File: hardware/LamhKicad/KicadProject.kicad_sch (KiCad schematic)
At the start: 45 parts, among them J1 JTAG-10 PIN, J2 436500303, J3 436500303, J4 436500303, J5 ESQ-110-X-X-D, J6 436500303, U1 TJA1051T-3, U2 PCA9685PW_112, U3 TLV70433DBVT, U4 STM32F072C8Tx

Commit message: ready to route
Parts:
- added C18, C19, C20: 1000uf 16v, Capacitor_THT:CP_Radial_D10.0mm_P5.00mm, symbol Device:C_Polarized_US
- C16: value 4700uf 16v -> 1000uf 16v; footprint (none) -> Capacitor_THT:CP_Radial_D10.0mm_P5.00mm
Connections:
- net 5v_SERVO: now also C18.1, C19.1, C20.1
- net GND: now also C18.2, C19.2, C20.2
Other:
- moved on the sheet: C16, J1

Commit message: fixed the connector
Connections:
- net NRST4: no longer J5.12
- net SWCLK: no longer J5.17
- new net NRST: J5.17
- new net SWCLK4: J5.12
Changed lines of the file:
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@@
-		)
-	)
-	(global_label "NRST2"
-		(shape input)
-		(at 195.58 198.12 0)
-		(fields_autoplaced yes)
-		(effects
-			(font
-				(size 1.27 1.27)
-			)
-			(justify left)
-		)
-		(property "Intersheetrefs" "${INTERSHEET_REFS}"
-			(at 204.5523 198.12 0)
-			(effects
-				(font
-					(size 1.27 1.27)
-				)
-				(justify left)
-				(hide yes)
-			)
 		)
 	)
@@
 		)
 	)
-	(global_label "NRST3"
-		(shape input)
-		(at 167.64 200.66 180)
-		(fields_autoplaced yes)
-		(effects
-			(font
-				(size 1.27 1.27)
-			)
-			(justify right)
-		)
-		(property "Intersheetrefs" "${INTERSHEET_REFS}"
-			(at 158.6677 200.66 0)
-			(effects
-				(font
-					(size 1.27 1.27)
-				)
-				(justify right)
-				(hide yes)
-			)
-		)
-	)
 	(global_label "3.3V"
 		(shape input)
@@
 		)
 	)
-	(global_label "NRST5"
-		(shape input)
-		(at 167.64 203.2 180)
-		(fields_autoplaced yes)
-		(effects
-			(font
-				(size 1.27 1.27)
-			)
-			(justify right)
-		)
-		(property "Intersheetrefs" "${INTERSHEET_REFS}"
-			(at 158.6677 203.2 0)
-			(effects
-				(font
-					(size 1.27 1.27)
-				)
-				(justify right)
-				(hide yes)
-			)
-		)
-	)
 	(global_label "MOSI"
 		(shape input)
@@
 		)
 	)
+	(global_label "NRST"
+		(shape input)
+		(at 168.91 208.28 180)
+		(fields_autoplaced yes)
+		(effects
+			(font
+				(size 1.27 1.27)
+			)
+			(justify right)
+		)
+		(property "Intersheetrefs" "${INTERSHEET_REFS}"
+			(at 161.1472 208.28 0)
+			(effects
+				(font
+					(size 1.27 1.27)
+				)
+				(justify right)
+				(hide yes)
+			)
+		)
+	)
 	(global_label "SWCLK"
 		(shape input)
-		(at 168.91 208.28 180)
-		(fields_autoplaced yes)
-		(effects
-			(font
-				(size 1.27 1.27)
-			)
-			(justify right)
-		)
-		(property "Intersheetrefs" "${INTERSHEET_REFS}"
-			(at 159.6958 208.28 0)
-			(effects
-				(font
-					(size 1.27 1.27)
-				)
-				(justify right)
-				(hide yes)
-			)
-		)
-	)
-	(global_label "SWCLK"
-		(shape input)
 		(at 243.84 106.68 180)
 		(fields_autoplaced yes)
@@
 		)
 	)
-	(global_label "NRST1"
-		(shape input)
-		(at 167.64 198.12 180)
-		(fields_autoplaced yes)
-		(effects
-			(font
-				(size 1.27 1.27)
-			)
-			(justify right)
-		)
-		(property "Intersheetrefs" "${INTERSHEET_REFS}"
-			(at 158.6677 198.12 0)
-			(effects
-				(font
-					(size 1.27 1.27)
-				)
-				(justify right)
-				(hide yes)
-			)
-		)
-	)
 	(global_label "3.3V"
 		(shape input)
@@
 		)
 	)
-	(global_label "NRST4"
+	(global_label "SWCLK4"
 		(shape input)
 		(at 194.31 200.66 0)
@@
 		)
 		(property "Intersheetrefs" "${INTERSHEET_REFS}"
-			(at 203.2823 200.66 0)
-			(effects
-				(font
+			(at 204.7337 200.66 0)
+			(effects
+				(font

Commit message: minor changes
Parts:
- added R14, R15: 10kΩ, Resistor_SMD:R_0402_1005Metric, symbol Device:R
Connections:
- net 3.3V: now also R15.2
- net GND: now also R14.2
- net NRST: now also U4.7 (NRST), R15.1
- net NRST4: no longer U4.7 (NRST)
- net at U4.44 (BOOT0): now also R14.1

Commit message: minor changes
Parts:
- removed R15: 10kΩ, Resistor_SMD:R_0402_1005Metric, symbol Device:R
- added C21: 100nF, Capacitor_SMD:C_0402_1005Metric, symbol Device:C
- added C27, C28: 8pF, Capacitor_SMD:C_0402_1005Metric, symbol Device:C
- added XTAL1: NX3225GD-8MHZ-STD-CRA-3, XTAL_NX3225GD-8MHZ-STD-CRA-3_NDK, symbol STDCRA38M:NX3225GD-8MHZ-STD-CRA-3
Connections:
- net CAN_o+ is gone; now on net CAN_+: J5.16
- net CAN_o- is gone; now on net CAN_-: J5.18
- net NRST4 is gone; now on net NRST: J1.1 (Pin_1)
- net SWCLK is gone; now on net SWCLK4: J1.2 (Pin_2), U4.3 (PC14)
- net CAN_+: no longer U1.1 (TXD), U4.33 (PA12)
- net CAN_-: no longer U1.4 (RXD), U4.32 (PA11)
- net GND: now also C21.2, C27.1, C28.2
- net NRST: now also C21.1
- net at R3.1: now also J2.1; no longer J4.1
- net at R3.2: now also U2.10 (LED4); no longer U2.8 (LED2)
- net at U4.5 (PF0): now also C27.2, XTAL1.1
- net at U4.6 (PF1): now also C28.1, XTAL1.2
- net at U2.12 (LED6): now also R6.2
- net at U2.7 (LED1): no longer R2.2
- net at U2.9 (LED3): no longer R6.2
- net at R1.1: now also J4.1; no longer J2.1
- net at J3.1: now also R6.1; no longer R2.1
- net at J6.1: now also R2.1; no longer R6.1
- net ADC: no longer names the net of U4.14 (PA4)
- net CLK: no longer names the net of U4.15 (PA5)
- net CS: no longer names the net of U4.11 (PA1)
- net MISO: no longer names the net of U4.16 (PA6)
- net MOSI: no longer names the net of U4.17 (PA7)
- net OE: no longer names the net of U4.12 (PA2)
- net RESET: no longer names the net of U4.13 (PA3)
- new net: R2.2, U2.8 (LED2)
- new net CAN_e+: U1.1 (TXD), U4.33 (PA12)
- new net CAN_e-: U1.4 (RXD), U4.32 (PA11)
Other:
- moved on the sheet: J1

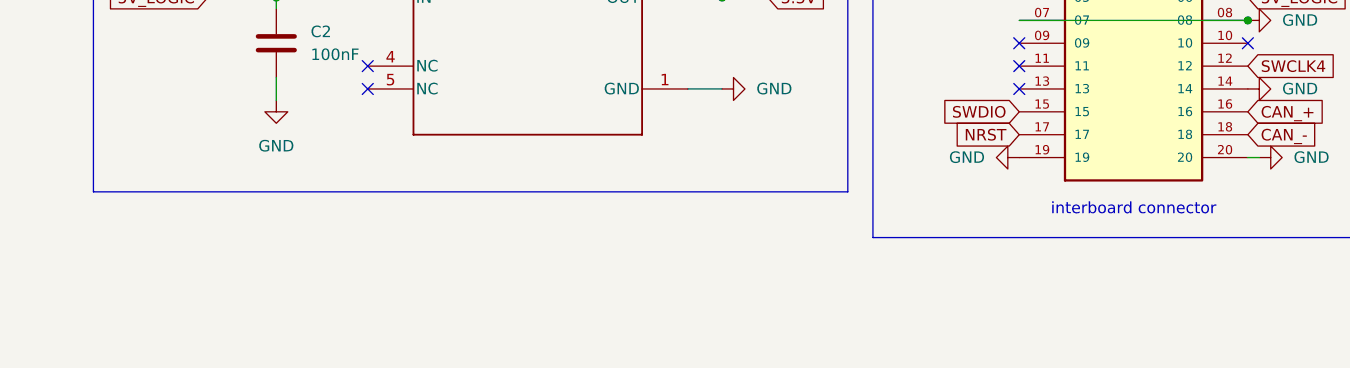
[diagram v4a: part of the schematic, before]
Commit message: added links to servo connectors
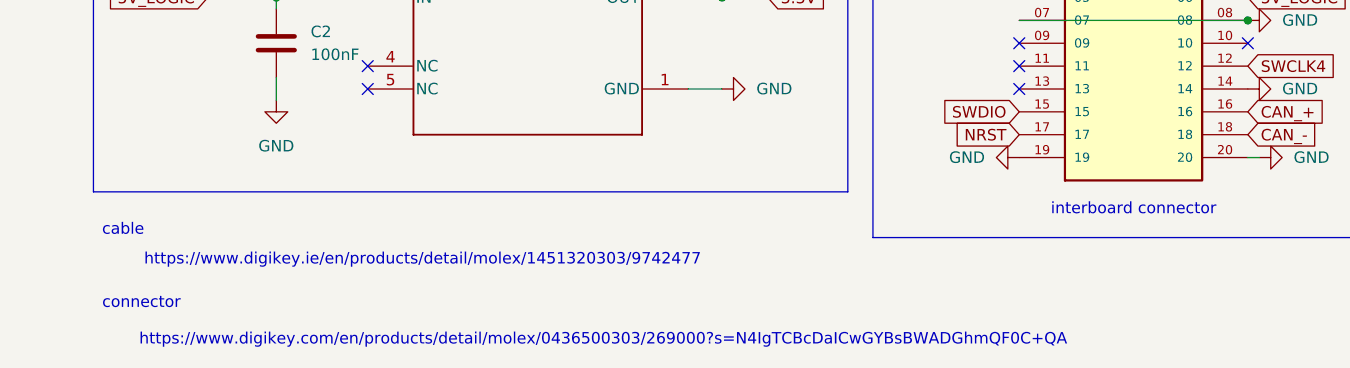
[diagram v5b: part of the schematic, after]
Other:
- note added: "cable"
- note added: "connector"
- note added: "https://www.digikey.com/en/products/detail/molex/0436500303/269000?s=N4IgTCBcDaICwGYBsBWADGhmQF0C+QA"
- note added: "https://www.digikey.ie/en/products/detail/molex/1451320303/9742477"
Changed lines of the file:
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@@
+		)
+	)
+	(text "cable\n"
+		(exclude_from_sim no)
+		(at 69.342 218.948 0)
+		(effects
+			(font
+				(size 1.27 1.27)
+			)
 		)
 	)
@@
 		(effects
 			(font
+				(size 1.27 1.27)
+			)
+		)
+	)
+	(text "https://www.digikey.com/en/products/detail/molex/0436500303/269000?s=N4IgTCBcDaICwGYBsBWADGhmQF0C+QA"
+		(exclude_from_sim no)
+		(at 122.682 231.14 0)
+		(effects
+			(font
+				(size 1.27 1.27)
+			)
+		)
+	)
+	(text "https://www.digikey.ie/en/products/detail/molex/1451320303/9742477"
+		(exclude_from_sim no)
+		(at 102.616 222.25 0)
+		(effects
+			(font
+				(size 1.27 1.27)
+			)
+		)
+	)
+	(text "connector\n"
+		(exclude_from_sim no)
+		(at 71.374 227.076 0)
+		(effects
+			(font

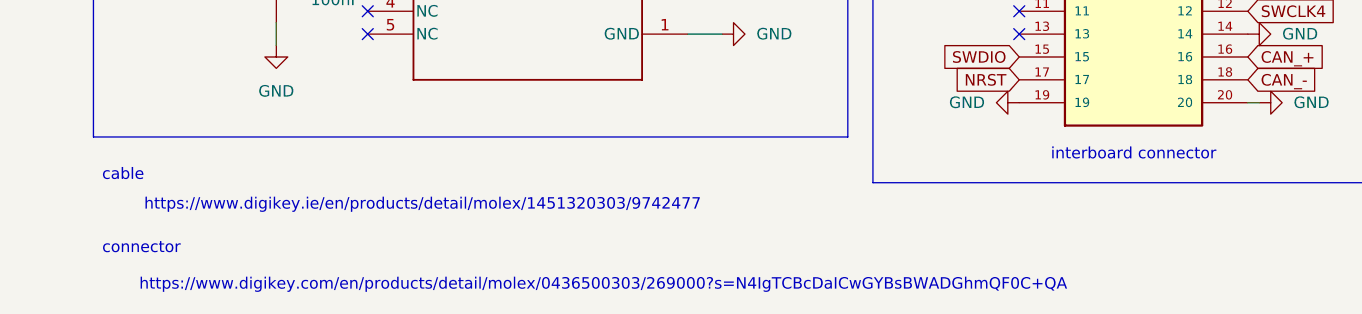
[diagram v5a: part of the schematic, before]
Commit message: thermal expansion vias
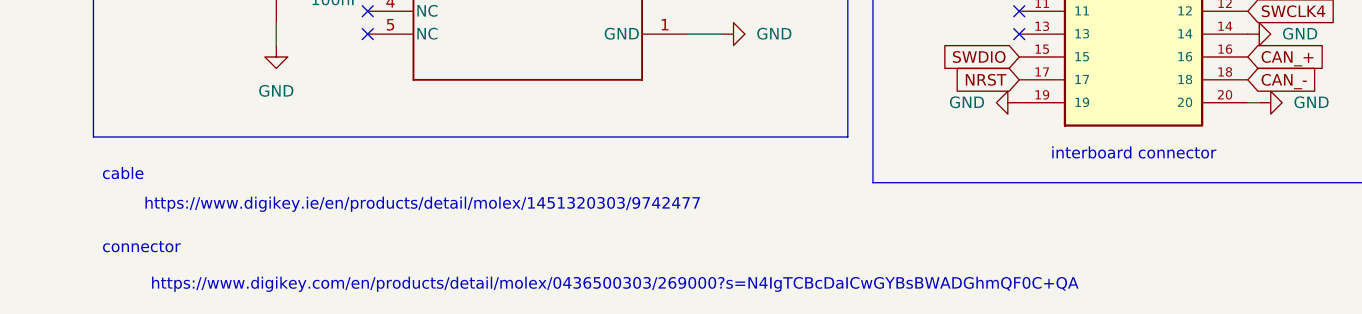
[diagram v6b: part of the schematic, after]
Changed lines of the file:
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@@
 	(text "https://www.digikey.com/en/products/detail/molex/0436500303/269000?s=N4IgTCBcDaICwGYBsBWADGhmQF0C+QA"
 		(exclude_from_sim no)
-		(at 122.682 231.14 0)
+		(at 123.952 231.14 0)
 		(effects
 			(font

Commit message: mockup done, must finish routing
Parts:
- removed C2: 100nF, Capacitor_SMD:C_0402_1005Metric, symbol Device:C
- removed C5: 100uF, Capacitor_SMD:C_0402_1005Metric, symbol Device:C
- removed J1: JTAG-10 PIN, Connector_IDC:IDC-Header_2x05_P2.54mm_Vertical, symbol Connector_Generic_MountingPin:Conn_01x10_MountingPin
- removed U3: TLV70433DBVT, DBV0005A_N, symbol TLV70433DBVT:TLV70433DBVT
- added 3v3, C+1, C-1, GND1, S1, S2, S3, S4: S2761-46R, HARWIN_S2761-46R, symbol S2761-46R:S2761-46R
- added J1: 5023860570, MOLEX_5023860570, symbol 5023860570:5023860570
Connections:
- net 3.3V: now also 3v3.1, J1.4
- net 5V_LOGIC: now also J5.11, J5.12; no longer J5.05, J5.06
- net 5v_SERVO: now also J5.03, J5.04, J5.05, J5.06, J5.07, J5.08; no longer J5.01, J5.02
- net CAN_+: now also C+1.1
- net CAN_-: now also C-1.1
- net GND: now also J5.01, J5.02, J5.09, J5.10, J5.13, J5.15, J5.17, GND1.1, J1.5, J1.S1 (SHIELD1), J1.S2 (SHIELD2); no longer J5.03, J5.04, J5.07, J5.08
- net NRST: now also J1.3; no longer J5.17
- net SWDIO: now also J1.2; no longer J5.15
- net at J2.1, R3.1: now also S3.1
- net at J3.1, R6.1: now also S4.1
- net at J6.1, R2.1: now also S2.1
- net at J4.1, R1.1: now also S1.1
- net SWCLK4 renamed SWCLK
- net SWCLK: now also J1.1; no longer J5.12
- no-connect marks 24 -> 14
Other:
- added sheet power (power.kicad_sch)

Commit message: clean asf
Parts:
- added 5VL1: S2761-46R, HARWIN_S2761-46R, symbol S2761-46R:S2761-46R
- added J7: EBBA-02-C-SS-BU, EBBA-02-C-SS-BU, symbol EBBA-02-C-SS-BU:EBBA-02-C-SS-BU
- added R18: 10kΩ, Resistor_SMD:R_0402_1005Metric, symbol Device:R
- renumbered S1 to PWM1, S2 to PWM2, S3 to PWM3, S4 to PWM4
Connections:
- net 5V_LOGIC: now also 5VL1.1
- net GND: now also J7.2 (02)
- net at U4.20 (PB2): now also J7.1 (01), R18.1
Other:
- note added: "our new battery connector for mach 2.5"
- note removed: "XT60PW-M, our new battery connector for mach 2.5"
- moved on the sheet: C14, C15, J1, PWM1
